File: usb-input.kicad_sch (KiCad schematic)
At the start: 7 parts, among them J3 USB_C_Receptacle_USB2.0_14P, U1 CH224K

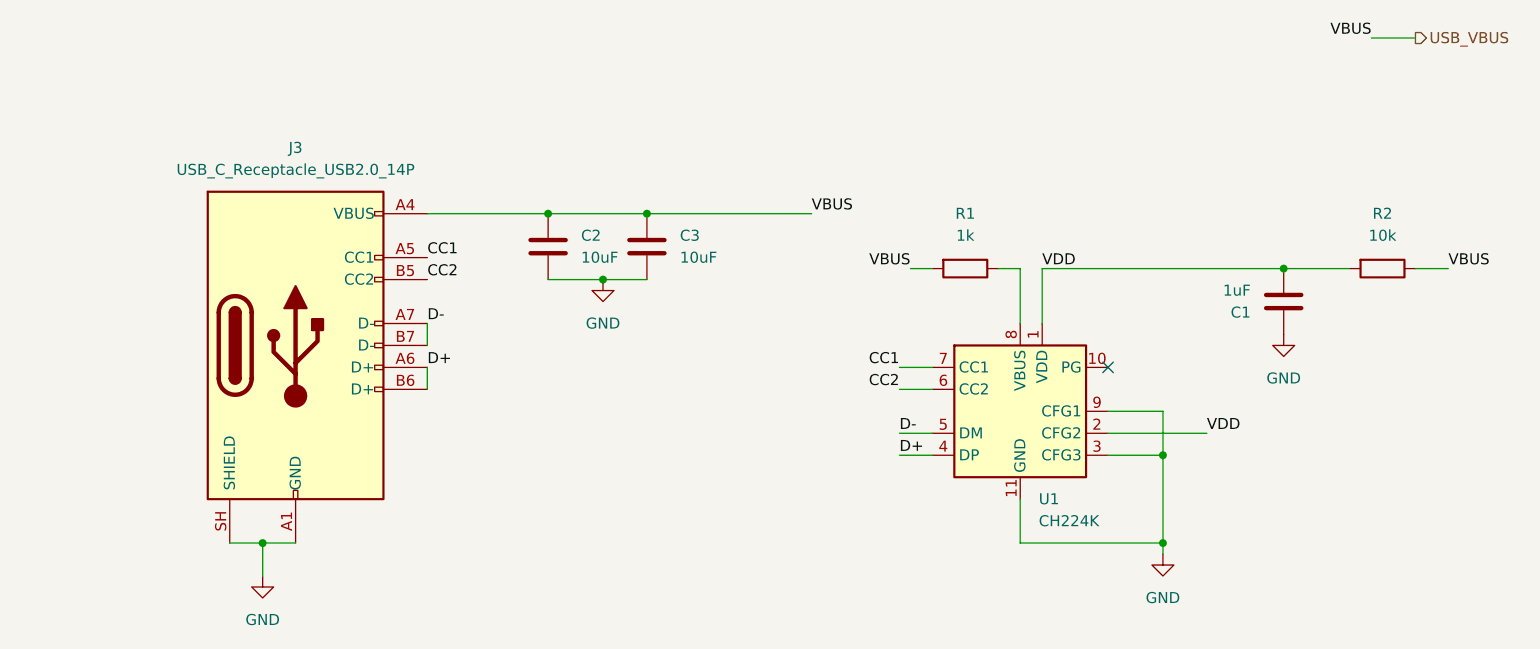
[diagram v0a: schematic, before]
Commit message: added ideal diode
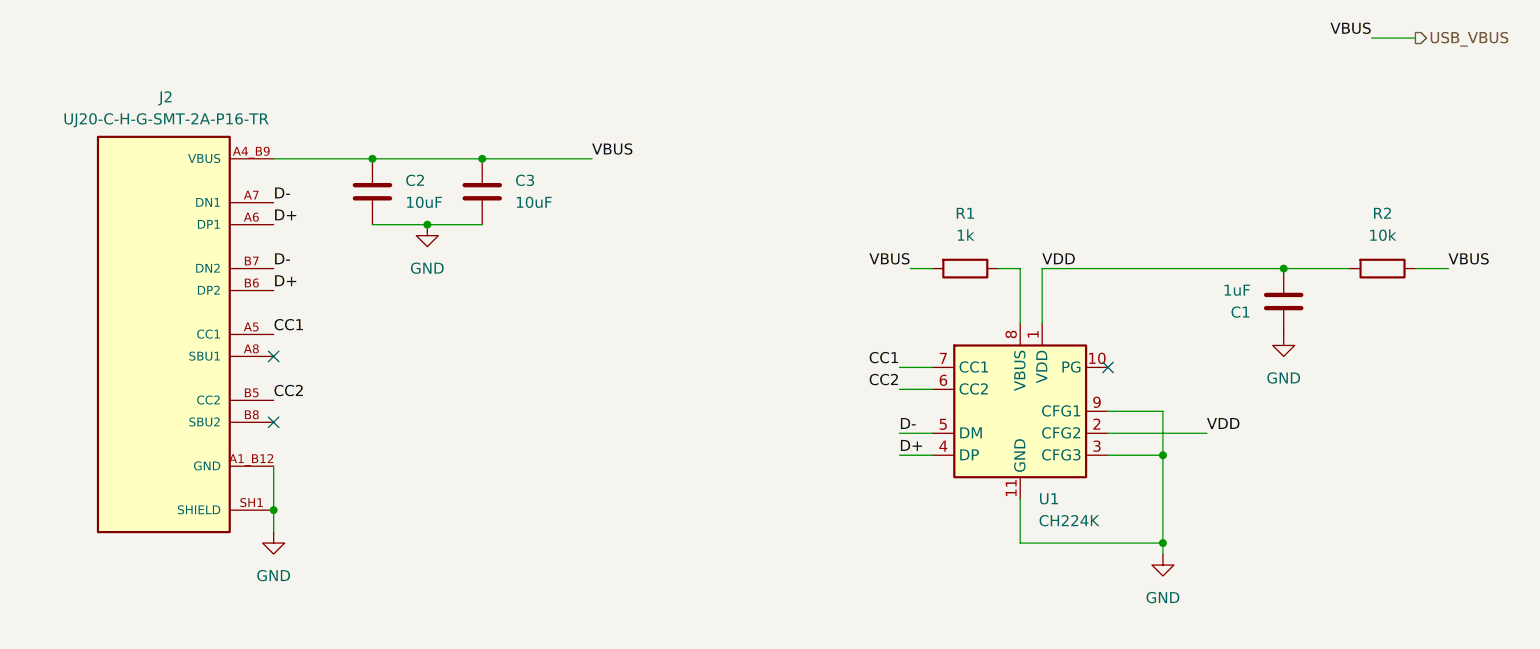
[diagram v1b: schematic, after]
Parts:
- removed J3: USB_C_Receptacle_USB2.0_14P, symbol Connector:USB_C_Receptacle_USB2.0_14P
- added J2: UJ20-C-H-G-SMT-2A-P16-TR, SnapEDA:SAMESKY_UJ20-C-H-G-SMT-2A-P16-TR, symbol Snapeda:UJ20-C-H-G-SMT-2A-P16-TR
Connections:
- net CC1: now also J2.A5 (CC1)
- net CC2: now also J2.B5 (CC2)
- net D+: now also J2.A6 (DP1), J2.B6 (DP2)
- net D-: now also J2.A7 (DN1), J2.B7 (DN2)
- net GND: now also J2.A1_B12 (GND), J2.B1_A12 (GND), J2.SH1 (SHIELD), J2.SH2 (SHIELD), J2.SH3 (SHIELD), J2.SH4 (SHIELD)
- net USB_VBUS renamed VBUS
- net VBUS: now also J2.A4_B9 (VBUS), J2.B4_A9 (VBUS)
- no-connect marks 1 -> 3
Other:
- moved on the sheet: C2, C3
